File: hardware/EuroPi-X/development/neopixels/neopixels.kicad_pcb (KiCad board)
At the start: 2 copper layers, 20.3 x 27.9 mm, 16 parts, among them J1 Conn_01x04_Pin, Q1 BSS138

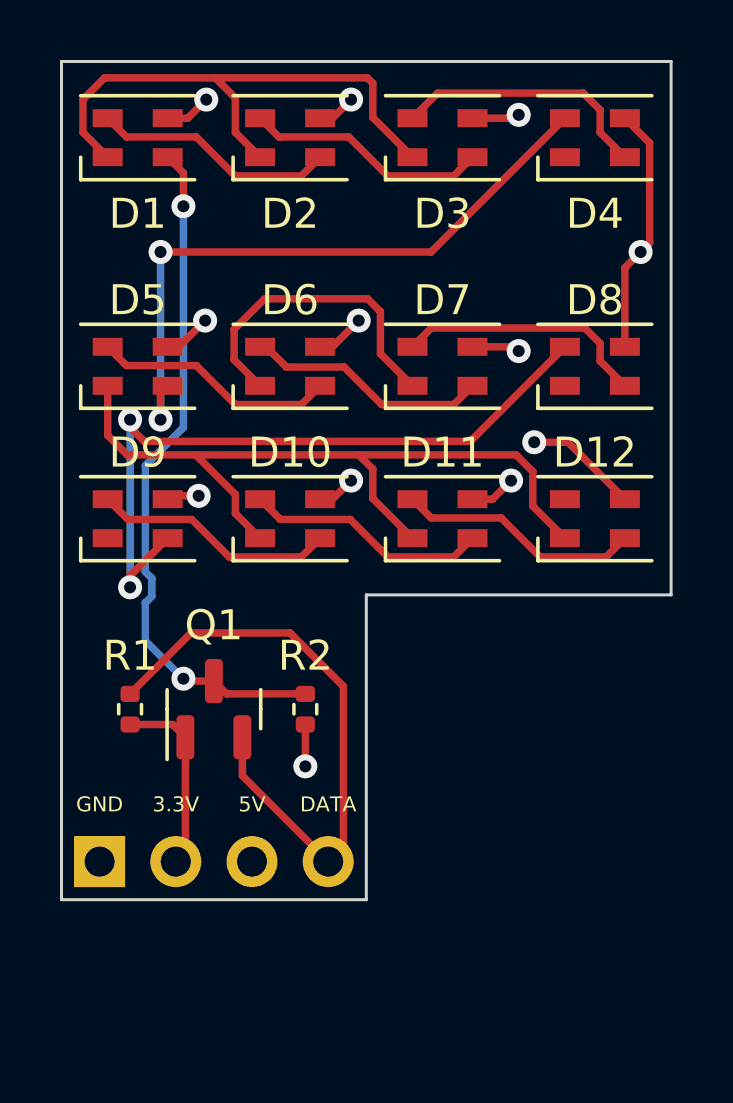
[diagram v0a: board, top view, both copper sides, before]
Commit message: rearrange neopixel dev board
make neopixel dev board 1u
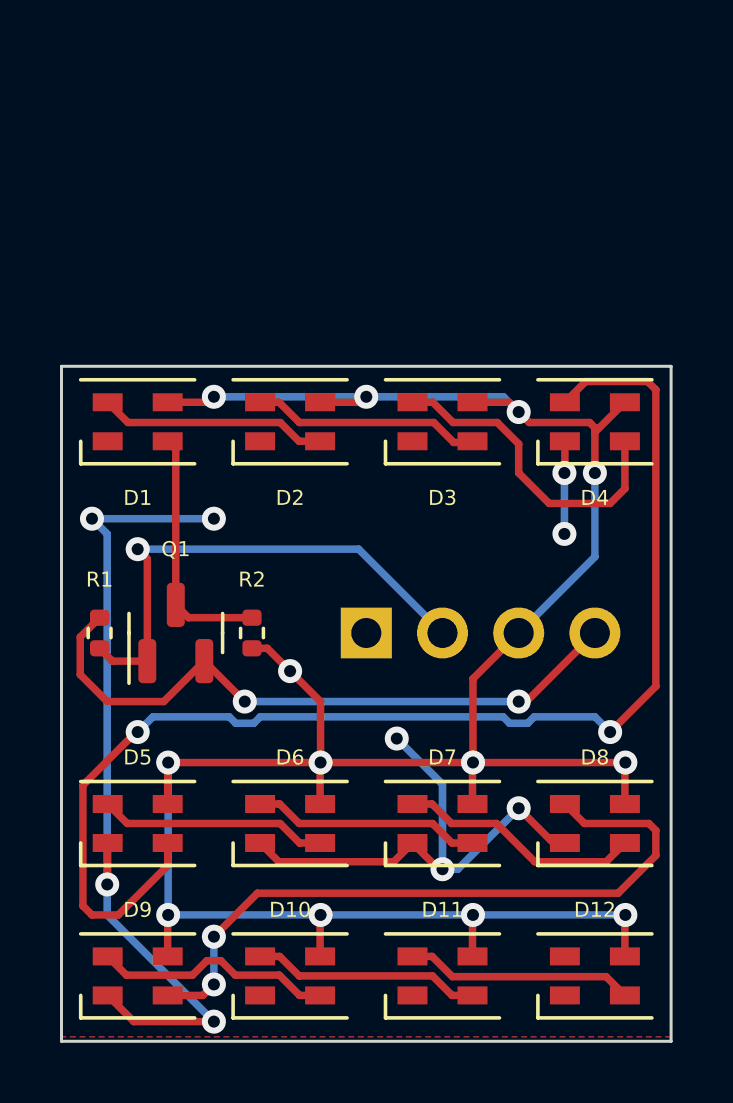
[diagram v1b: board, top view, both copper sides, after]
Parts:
- moved D10 15.2 mm to (7.62, 20.3)
- moved D11 15.2 mm to (12.7, 20.3)
- moved D12 15.2 mm to (17.8, 20.3)
- moved D5 15.2 mm to (2.54, 15.2)
- moved D6 15.2 mm to (7.62, 15.2)
- moved D7 15.2 mm to (12.7, 15.2)
- moved D8 15.2 mm to (17.8, 15.2)
- moved D9 15.2 mm to (2.54, 20.3)
- moved J1 11.7 mm to (10.2, 8.89)
- moved D1 9.47 mm to (2.54, 1.85)
- moved D2 9.47 mm to (7.62, 1.85)
- moved D3 9.47 mm to (12.7, 1.85)
- moved D4 9.47 mm to (17.8, 1.85)
- moved R2 3.10 mm to (6.35, 8.89)
- moved Q1 2.84 mm to (3.81, 8.89)
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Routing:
- net +5V: track 26.7 -> 84.0 mm, vias 12 -> 13
- net Net-(D4-DOUT): track 22.1 -> 43.0 mm
- net Net-(D1-DIN): track 23.1 -> 8.28 mm, vias 2 -> 0
- net +3.3V: track 6.30 -> 16.9 mm, vias 0 -> 1
- net Earth: track 55.4 -> 48.2 mm, vias 0 -> 9
- net Net-(D3-DOUT): track 8.75 -> 10.8 mm
- net /DATA_IN: track 20.1 -> 21.8 mm, vias 0 -> 2
- net Net-(D8-DOUT): track 24.0 -> 23.4 mm
- net Net-(D11-DOUT): track 8.14 -> 7.62 mm
- net Net-(D10-DOUT): track 8.14 -> 7.62 mm
- net Net-(D5-DOUT): track 8.14 -> 7.62 mm
- net Net-(D1-DOUT): track 8.14 -> 7.62 mm
- net Net-(D6-DOUT): track 8.14 -> 7.62 mm
- removed copper zone on B.Cu, net +5V
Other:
- board size 20.3 x 27.9 mm -> 20.3 x 22.5 mm
